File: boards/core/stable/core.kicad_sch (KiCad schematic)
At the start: 11 parts, among them J201 Conn_02x08_Counter_Clockwise, J202 Conn_02x08_Counter_Clockwise, J203 Conn_02x08_Counter_Clockwise, J204 Conn_02x08_Counter_Clockwise, J214 Conn_02x04_Counter_Clockwise

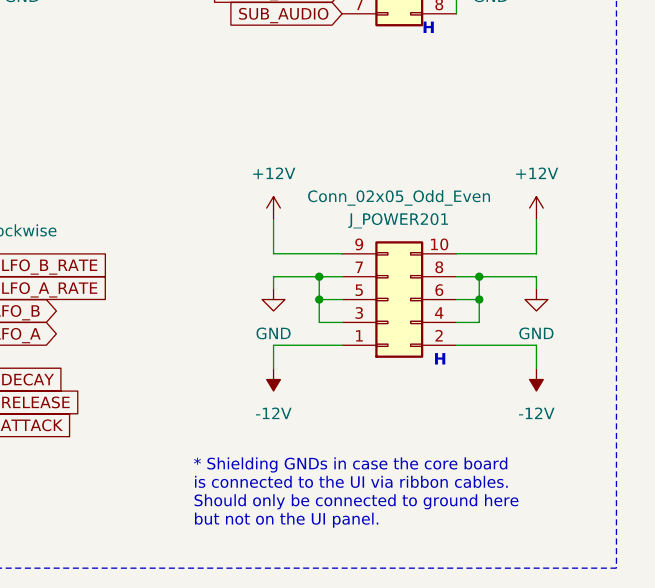
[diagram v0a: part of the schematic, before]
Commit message: Streamline 'Stable' Core board
https://github.com/shmoergh/hog/issues/7

- Remove 12V terminal input
- Reposition Eurorack power connector to right so it makes space for tuning
- Remove all unnecessary thermal compensation pseudo components
- Reposition tuning trimmers
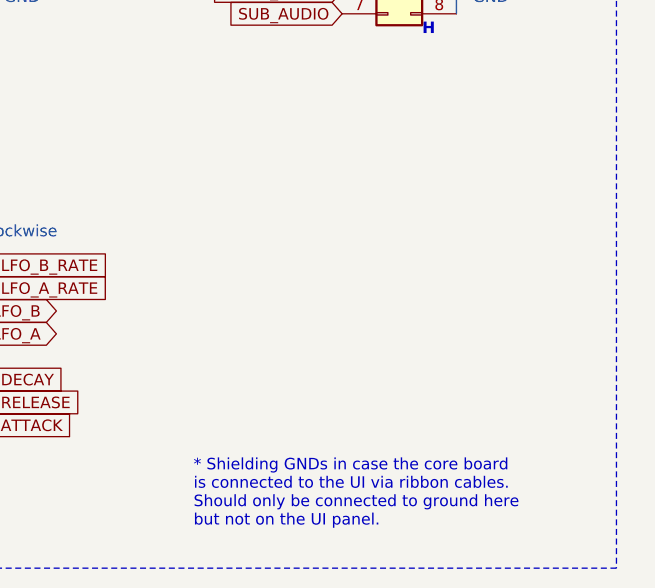
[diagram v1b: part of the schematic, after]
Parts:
- removed J_POWER201: Conn_02x05_Odd_Even, Connector_IDC:IDC-Header_2x05_P2.54mm_Vertical, symbol Connector_Generic:Conn_02x05_Odd_Even
- J201, J202, J203, J204: footprint Connector_IDC:IDC-Header_2x08_P2.54mm_Vertical -> Connector_PinHeader_2.54mm:PinHeader_2x08_P2.54mm_Vertical

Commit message: Updated and checked Core board BOM
ref https://github.com/shmoergh/hog/issues/19
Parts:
- J201, J202, J203, J204: Part No. (none) -> 737-RS2-16-G; Part URL (none) -> https://mou.sr/3OWyRwS; Vendor (none) -> Mouser; now in the parts list
- J214: Part No. (none) -> 737-RS2-08-G; Part URL (none) -> https://mou.sr/41qYCwK; Vendor (none) -> Mouser; now in the parts list
